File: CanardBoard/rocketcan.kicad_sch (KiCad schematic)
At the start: 21 parts, among them J6 G125-MH104M4-04AD000P, U15 TPS2521, U17 TCAN3413DDFR

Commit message: done
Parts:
- removed D19: RB520S30T1G, Diode_SMD:D_SOD-523, symbol Device:D_Schottky
- removed R28: 31.6k, Resistor_SMD:R_0402_1005Metric, symbol Device:R_Small_US
- removed R30: 100k, Resistor_SMD:R_0402_1005Metric, symbol Device_Custom:R_Small_US
- C51: symbol Device_Custom:C_Small -> Device:C_Small
- C52: renamed from C59; symbol Device_Custom:C_Small -> Device:C_Small
- C53: renamed from C52; symbol Device_Custom:C_Small -> Device:C_Small
- C54: renamed from C72; symbol Device_Custom:C_Small -> Device:C_Small
- C55: renamed from C73; symbol Device_Custom:C_Small -> Device:C_Small
- C56: renamed from C60; symbol Device_Custom:C_Small -> Device:C_Small
- R44: renamed from R56; symbol Device_Custom:R_Small_US -> Device:R_Small_US
- R45: renamed from R57; symbol Device_Custom:R_Small_US -> Device:R_Small_US
- R46: renamed from R58; symbol Device_Custom:R_Small_US -> Device:R_Small_US
- R47: renamed from R54; symbol Device_Custom:R_Small_US -> Device:R_Small_US
- R48: renamed from R43; footprint Resistor_SMD:R_0402_1005Metric -> Resistor_SMD:R_0805_2012Metric; symbol Device_Custom:R_Small_US -> Device:R_Small_US
- R49: renamed from R48; symbol Device_Custom:R_Small_US -> Device:R_Small_US
- renumbered D1 to D16, F2 to F8, F1 to F9, J6 to J10, U17 to U15, U15 to U16
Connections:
- net 5V_EXT_EN renamed EN_EXT_5V
- net 5V_EXT_FLT renamed FLT_EXT_5V

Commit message: changes
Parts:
- renumbered D16 to D18, R44 to R43, R45 to R44, R46 to R45, R47 to R46, R48 to R47, R49 to R48
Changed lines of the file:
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@@
 		(on_board yes)
 		(dnp yes)
-		(property "Reference" "R48"
+		(property "Reference" "R47"
 			(at 142.24 132.08 90)
 			(effects
@@
 			(project "CanardBoard"
 				(path "/605ab838-6b02-4cf5-a6b5-94a0cdb1b998/4fea5507-ad74-497c-bf16-b3654a0fa101"
-					(reference "R48")
+					(reference "R47")
 					(unit 1)
 				)
@@
 		(dnp no)
 		(fields_autoplaced yes)
-		(property "Reference" "#PWR0136"
+		(property "Reference" "#PWR0139"
 			(at 181.61 97.79 0)
 			(effects
@@
 			(project "CanardBoard"
 				(path "/605ab838-6b02-4cf5-a6b5-94a0cdb1b998/4fea5507-ad74-497c-bf16-b3654a0fa101"
-					(reference "#PWR0136")
+					(reference "#PWR0139")
 					(unit 1)
 				)
@@
 		(on_board yes)
 		(dnp no)
-		(property "Reference" "R47"
+		(property "Reference" "R46"
 			(at 133.35 86.36 90)
 			(effects
@@
 			(project "CanardBoard"
 				(path "/605ab838-6b02-4cf5-a6b5-94a0cdb1b998/4fea5507-ad74-497c-bf16-b3654a0fa101"
-					(reference "R47")
+					(reference "R46")
 					(unit 1)
 				)
@@
 		(dnp no)
 		(fields_autoplaced yes)
-		(property "Reference" "#PWR0124"
+		(property "Reference" "#PWR0127"
 			(at 74.93 87.63 0)
 			(effects
@@
 			(project "CanardBoard"
 				(path "/605ab838-6b02-4cf5-a6b5-94a0cdb1b998/4fea5507-ad74-497c-bf16-b3654a0fa101"
-					(reference "#PWR0124")
+					(reference "#PWR0127")
 					(unit 1)
 				)
@@
 		(dnp no)
 		(fields_autoplaced yes)
-		(property "Reference" "#PWR0137"
+		(property "Reference" "#PWR0140"
 			(at 189.23 97.79 0)
 			(effects
@@
 			(project "CanardBoard"
 				(path "/605ab838-6b02-4cf5-a6b5-94a0cdb1b998/4fea5507-ad74-497c-bf16-b3654a0fa101"
-					(reference "#PWR0137")
+					(reference "#PWR0140")
 					(unit 1)
 				)
@@
 		(dnp no)
 		(fields_autoplaced yes)
-		(property "Reference" "#PWR0126"
+		(property "Reference" "#PWR0129"
 			(at 81.28 149.86 0)
 			(effects
@@
 			(project "CanardBoard"
 				(path "/605ab838-6b02-4cf5-a6b5-94a0cdb1b998/4fea5507-ad74-497c-bf16-b3654a0fa101"
-					(reference "#PWR0126")
+					(reference "#PWR0129")
 					(unit 1)
 				)
@@
 		(dnp no)
 		(fields_autoplaced yes)
-		(property "Reference" "#PWR0131"
+		(property "Reference" "#PWR0134"
 			(at 125.73 129.54 0)
 			(effects
@@
 			(project "CanardBoard"
 				(path "/605ab838-6b02-4cf5-a6b5-94a0cdb1b998/4fea5507-ad74-497c-bf16-b3654a0fa101"
-					(reference "#PWR0131")
+					(reference "#PWR0134")
 					(unit 1)
 				)
@@
 		(dnp no)
 		(fields_autoplaced yes)
-		(property "Reference" "#PWR0134"
+		(property "Reference" "#PWR0137"
 			(at 156.21 161.29 0)
 			(effects
@@
 			(project "CanardBoard"
 				(path "/605ab838-6b02-4cf5-a6b5-94a0cdb1b998/4fea5507-ad74-497c-bf16-b3654a0fa101"
-					(reference "#PWR0134")
+					(reference "#PWR0137")
 					(unit 1)
 				)
@@
 		(on_board yes)
 		(dnp no)
-		(property "Reference" "R49"
+		(property "Reference" "R48"
 			(at 185.42 68.58 90)
 			(effects
@@
 			(project "CanardBoard"
 				(path "/605ab838-6b02-4cf5-a6b5-94a0cdb1b998/4fea5507-ad74-497c-bf16-b3654a0fa101"
-					(reference "R49")
+					(reference "R48")
 					(unit 1)
 				)
@@
 		(dnp no)
 		(fields_autoplaced yes)
-		(property "Reference" "#PWR0132"
+		(property "Reference" "#PWR0135"
 			(at 135.89 57.15 0)
 			(effects
@@
 			(project "CanardBoard"
 				(path "/605ab838-6b02-4cf5-a6b5-94a0cdb1b998/4fea5507-ad74-497c-bf16-b3654a0fa101"
-					(reference "#PWR0132")
+					(reference "#PWR0135")
 					(unit 1)
 				)
@@
 		(dnp no)
 		(fields_autoplaced yes)
-		(property "Reference" "#PWR0138"
+		(property "Reference" "#PWR0141"
 			(at 200.66 97.79 0)
 			(effects
@@
 			(project "CanardBoard"
 				(path "/605ab838-6b02-4cf5-a6b5-94a0cdb1b998/4fea5507-ad74-497c-bf16-b3654a0fa101"
-					(reference "#PWR0138")
+					(reference "#PWR0141")
 					(unit 1)
 				)
@@
 		(on_board yes)
 		(dnp no)
-		(property "Reference" "R44"
+		(property "Reference" "R43"
 			(at 113.03 71.12 90)
 			(effects
@@
 			(project "CanardBoard"
 				(path "/605ab838-6b02-4cf5-a6b5-94a0cdb1b998/4fea5507-ad74-497c-bf16-b3654a0fa101"
-					(reference "R44")
+					(reference "R43")
 					(unit 1)
 				)
@@
 		(dnp no)
 		(fields_autoplaced yes)
-		(property "Reference" "#PWR0127"
+		(property "Reference" "#PWR0130"
 			(at 90.17 54.61 0)
 			(effects
@@
 			(project "CanardBoard"
 				(path "/605ab838-6b02-4cf5-a6b5-94a0cdb1b998/4fea5507-ad74-497c-bf16-b3654a0fa101"
-					(reference "#PWR0127")
+					(reference "#PWR0130")
 					(unit 1)
 				)
@@
 		(dnp no)
 		(fields_autoplaced yes)
-		(property "Reference" "#PWR0123"
+		(property "Reference" "#PWR0126"
 			(at 74.93 54.61 0)
 			(effects
@@
 			(project "CanardBoard"
 				(path "/605ab838-6b02-4cf5-a6b5-94a0cdb1b998/4fea5507-ad74-497c-bf16-b3654a0fa101"
-					(reference "#PWR0123")
+					(reference "#PWR0126")
 					(unit 1)
 				)
@@
 		(dnp no)
 		(fields_autoplaced yes)
-		(property "Reference" "#PWR0125"
+		(property "Reference" "#PWR0128"
 			(at 81.28 114.3 0)
 			(effects
@@
 			(project "CanardBoard"
 				(path "/605ab838-6b02-4cf5-a6b5-94a0cdb1b998/4fea5507-ad74-497c-bf16-b3654a0fa101"
-					(reference "#PWR0125")
+					(reference "#PWR0128")
 					(unit 1)
 				)
@@
 		(dnp no)
 		(fields_autoplaced yes)
-		(property "Reference" "#PWR0130"
+		(property "Reference" "#PWR0133"
 			(at 116.84 114.3 0)
 			(effects
@@
 			(project "CanardBoard"
 				(path "/605ab838-6b02-4cf5-a6b5-94a0cdb1b998/4fea5507-ad74-497c-bf16-b3654a0fa101"
-					(reference "#PWR0130")
+					(reference "#PWR0133")
 					(unit 1)
 				)
@@
 		(on_board yes)
 		(dnp no)
-		(property "Reference" "R45"
+		(property "Reference" "R44"
 			(at 113.03 78.74 90)
 			(effects
@@
 			(project "CanardBoard"
 				(path "/605ab838-6b02-4cf5-a6b5-94a0cdb1b998/4fea5507-ad74-497c-bf16-b3654a0fa101"
-					(reference "R45")
+					(reference "R44")
 					(unit 1)
 				)
@@
 		(dnp no)
 		(fields_autoplaced yes)
-		(property "Reference" "#PWR0135"
+		(property "Reference" "#PWR0138"
 			(at 181.61 63.5 0)
 			(effects
@@
 			(project ""
 				(path "/605ab838-6b02-4cf5-a6b5-94a0cdb1b998/4fea5507-ad74-497c-bf16-b3654a0fa101"
-					(reference "#PWR0135")
+					(reference "#PWR0138")
 					(unit 1)
 				)
@@
 		(on_board yes)
 		(dnp no)
-		(property "Reference" "R46"
+		(property "Reference" "R45"
 			(at 133.35 59.69 90)
 			(effects
@@
 			(project "CanardBoard"
 				(path "/605ab838-6b02-4cf5-a6b5-94a0cdb1b998/4fea5507-ad74-497c-bf16-b3654a0fa101"
-					(reference "R46")
+					(reference "R45")
 					(unit 1)
 				)
@@
 		(dnp no)
 		(fields_autoplaced yes)
-		(property "Reference" "#PWR0139"
+		(property "Reference" "#PWR0142"
 			(at 205.74 78.74 0)
 			(effects
@@
 			(project "CanardBoard"
 				(path "/605ab838-6b02-4cf5-a6b5-94a0cdb1b998/4fea5507-ad74-497c-bf16-b3654a0fa101"
-					(reference "#PWR0139")
+					(reference "#PWR0142")
 					(unit 1)
 				)
@@
 		(dnp no)
 		(fields_autoplaced yes)
-		(property "Reference" "D16"
+		(property "Reference" "D18"
 			(at 162.56 144.7799 0)
 			(effects
@@
 			(project "CanardBoard"
 				(path "/605ab838-6b02-4cf5-a6b5-94a0cdb1b998/4fea5507-ad74-497c-bf16-b3654a0fa101"
-					(reference "D16")
+					(reference "D18")
 					(unit 1)
 				)
@@
 		(dnp no)
 		(fields_autoplaced yes)
-		(property "Reference" "#PWR0129"
+		(property "Reference" "#PWR0132"
 			(at 115.57 97.79 0)
 			(effects
@@
 			(project "CanardBoard"
 				(path "/605ab838-6b02-4cf5-a6b5-94a0cdb1b998/4fea5507-ad74-497c-bf16-b3654a0fa101"
-					(reference "#PWR0129")
+					(reference "#PWR0132")
 					(unit 1)
 				)
@@
 		(dnp no)
 		(fields_autoplaced yes)
-		(property "Reference" "#PWR0122"
+		(property "Reference" "#PWR0125"
 			(at 71.12 129.54 0)
 			(effects
@@
 			(project "CanardBoard"
 				(path "/605ab838-6b02-4cf5-a6b5-94a0cdb1b998/4fea5507-ad74-497c-bf16-b3654a0fa101"
-					(reference "#PWR0122")
+					(reference "#PWR0125")
 					(unit 1)
 				)
@@
 		(dnp no)
 		(fields_autoplaced yes)
-		(property "Reference" "#PWR0128"
+		(property "Reference" "#PWR0131"
 			(at 90.17 87.63 0)
 			(effects
@@
 			(project "CanardBoard"
 				(path "/605ab838-6b02-4cf5-a6b5-94a0cdb1b998/4fea5507-ad74-497c-bf16-b3654a0fa101"
-					(reference "#PWR0128")
+					(reference "#PWR0131")
 					(unit 1)
 				)
@@
 		(dnp no)
 		(fields_autoplaced yes)
-		(property "Reference" "#PWR0133"
+		(property "Reference" "#PWR0136"
 			(at 135.89 97.79 0)
 			(effects
@@
 			(project "CanardBoard"
 				(path "/605ab838-6b02-4cf5-a6b5-94a0cdb1b998/4fea5507-ad74-497c-bf16-b3654a0fa101"
-					(reference "#PWR0133")
-					(unit 1)
-				)
+					(reference "#PWR0136")
+					(unit 1)
+				)

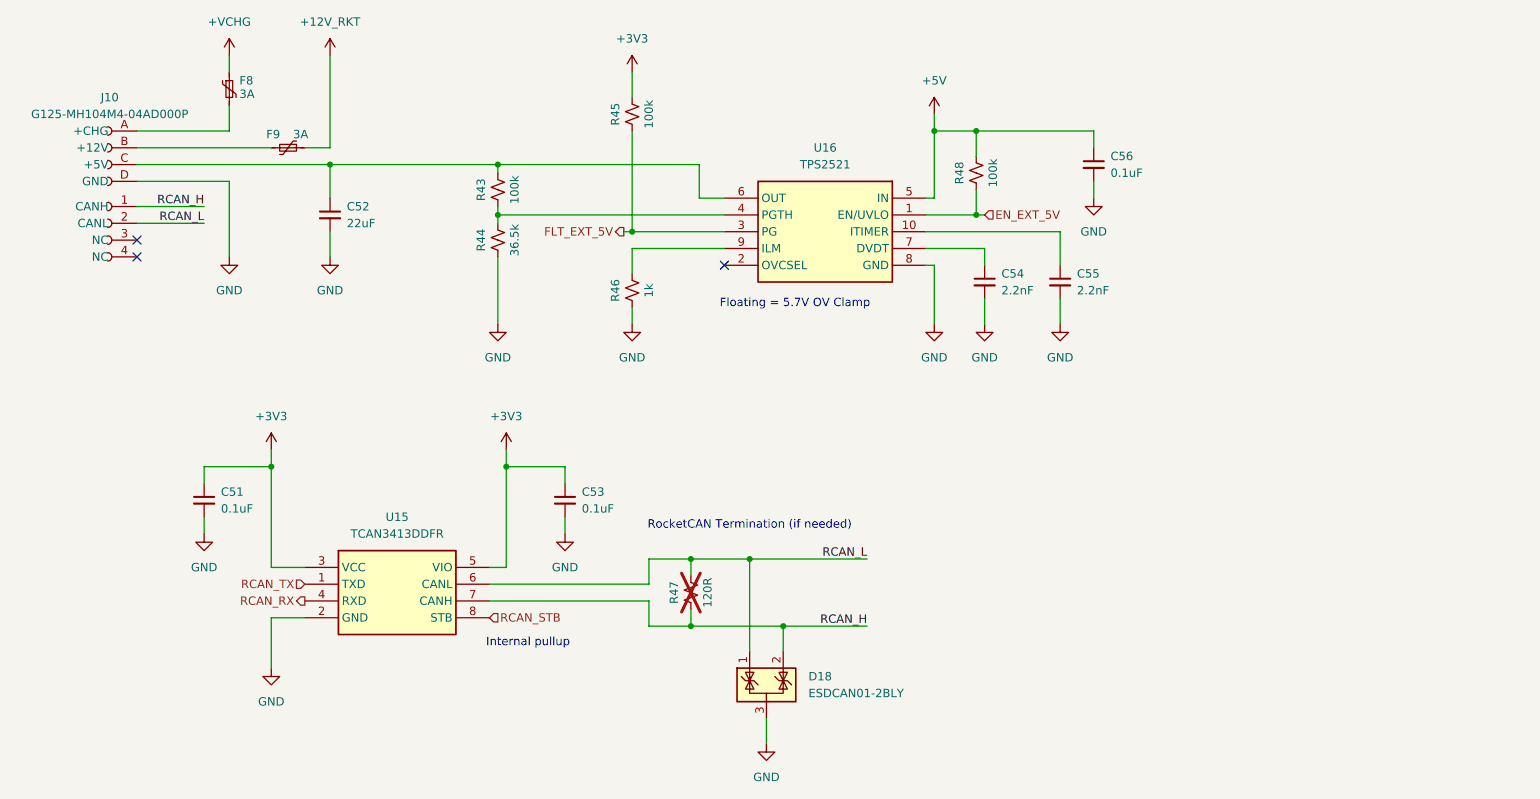
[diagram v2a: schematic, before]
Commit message: found new components to simplify and make board smaller
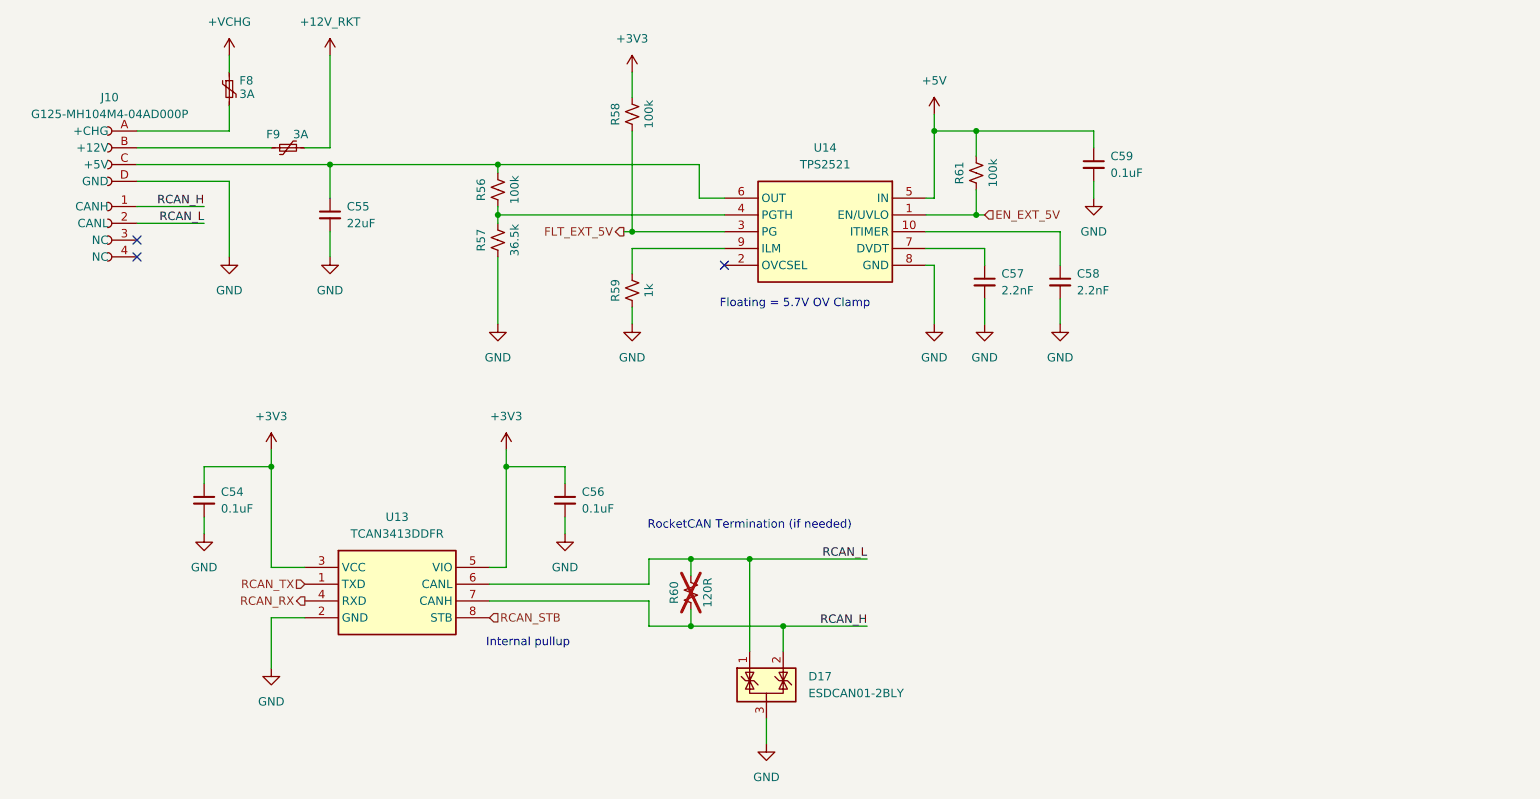
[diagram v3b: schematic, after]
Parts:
- renumbered C51 to C54, C52 to C55, C53 to C56, C54 to C57, C55 to C58, C56 to C59, D18 to D17, R43 to R56, R44 to R57, R45 to R58, R46 to R59, R47 to R60, R48 to R61, U15 to U13, U16 to U14

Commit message: work
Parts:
- renumbered C54 to C55, C55 to C56, C56 to C57, C57 to C58, C58 to C59, C59 to C60
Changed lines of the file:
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@@
 		(dnp no)
 		(fields_autoplaced yes)
-		(property "Reference" "C58"
+		(property "Reference" "C59"
 			(at 203.2 83.8262 0)
 			(effects
@@
 			(project "CanardBoard"
 				(path "/605ab838-6b02-4cf5-a6b5-94a0cdb1b998/4fea5507-ad74-497c-bf16-b3654a0fa101"
-					(reference "C58")
+					(reference "C59")
 					(unit 1)
 				)
@@
 		(dnp no)
 		(fields_autoplaced yes)
-		(property "Reference" "C56"
+		(property "Reference" "C57"
 			(at 128.27 116.8462 0)
 			(effects
@@
 			(project "CanardBoard"
 				(path "/605ab838-6b02-4cf5-a6b5-94a0cdb1b998/4fea5507-ad74-497c-bf16-b3654a0fa101"
-					(reference "C56")
+					(reference "C57")
 					(unit 1)
 				)
@@
 		(dnp no)
 		(fields_autoplaced yes)
-		(property "Reference" "C59"
+		(property "Reference" "C60"
 			(at 208.28 66.0462 0)
 			(effects
@@
 			(project "CanardBoard"
 				(path "/605ab838-6b02-4cf5-a6b5-94a0cdb1b998/4fea5507-ad74-497c-bf16-b3654a0fa101"
-					(reference "C59")
+					(reference "C60")
 					(unit 1)
 				)
@@
 		(dnp no)
 		(fields_autoplaced yes)
-		(property "Reference" "C57"
+		(property "Reference" "C58"
 			(at 191.77 83.8262 0)
 			(effects
@@
 			(project "CanardBoard"
 				(path "/605ab838-6b02-4cf5-a6b5-94a0cdb1b998/4fea5507-ad74-497c-bf16-b3654a0fa101"
-					(reference "C57")
+					(reference "C58")
 					(unit 1)
 				)
@@
 		(dnp no)
 		(fields_autoplaced yes)
-		(property "Reference" "C54"
+		(property "Reference" "C55"
 			(at 73.66 116.8462 0)
 			(effects
@@
 			(project "CanardBoard"
 				(path "/605ab838-6b02-4cf5-a6b5-94a0cdb1b998/4fea5507-ad74-497c-bf16-b3654a0fa101"
-					(reference "C54")
+					(reference "C55")
 					(unit 1)
 				)
@@
 		(dnp no)
 		(fields_autoplaced yes)
-		(property "Reference" "C55"
+		(property "Reference" "C56"
 			(at 92.71 73.6662 0)
 			(effects
@@
 			(project "CanardBoard"
 				(path "/605ab838-6b02-4cf5-a6b5-94a0cdb1b998/4fea5507-ad74-497c-bf16-b3654a0fa101"
-					(reference "C55")
-					(unit 1)
-				)
+					(reference "C56")
+					(unit 1)
+				)

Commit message: stuff
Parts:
- removed U14: TPS2521, canardboard:TPS2521, symbol canardboard:TPS2521
- added R62: 43.2k, Resistor_SMD:R_0402_1005Metric, symbol Device:R_Small_US
- added U14: TPS259472, canardboard:TPS25947xx, symbol canardboard:TPS259472
- C60: value 0.1uF -> 1uF
- R57: value 36.5k -> 34k
- R58: value 100k -> 681R
- R59: value 1k -> 100k
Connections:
- net FLT_EXT_5V is gone; now on net GND: R58.2
- net +3V3: now also R59.1; no longer R58.1
- net +5V: now also U14.5 (IN)
- net EN_EXT_5V: now also R62.1, U14.1 (EN/UVLO)
- net GND: now also R62.2, U14.8 (GND); no longer R59.2
- net at C59.1: now also U14.10 (ITIMER)
- net at C56.1, J10.C (+5V), R56.1: now also U14.6 (OUT)
- net at R56.2, R57.1: now also U14.4 (PGTH)
- net at C58.1: now also U14.7 (DVDT)
- new net: R58.1, U14.9 (ILM)
- new net PG_EXT_5V: R59.2, U14.3 (PG)

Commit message: more stuff
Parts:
- added C89: 22uF, Capacitor_SMD:C_0805_2012Metric, symbol Device:C_Small
- added C91: 0.1uF, Capacitor_SMD:C_0402_1005Metric, symbol Device:C_Small
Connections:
- net +5V: now also C91.1
- net GND: now also C89.2, C91.2
- net RKT_5V_OUT: now reaches C56.1, J10.C (+5V), R56.1, U14.6 (OUT)
- net RKT_5V_OUT: now also C89.1

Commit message: more work
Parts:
- added TP5: RCAN_H, TestPoint:TestPoint_Pad_D1.0mm, symbol Connector:TestPoint_Small
- added TP6: RCAN_L, TestPoint:TestPoint_Pad_D1.0mm, symbol Connector:TestPoint_Small
- added TP7: RCAN_RX, TestPoint:TestPoint_Pad_D1.0mm, symbol Connector:TestPoint_Small
- added TP8: RCAN_TX, TestPoint:TestPoint_Pad_D1.0mm, symbol Connector:TestPoint_Small
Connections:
- net RCAN_H: now also TP5.1
- net RCAN_L: now also TP6.1
- net RCAN_RX: now also TP7.1
- net RCAN_TX: now also TP8.1

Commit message: fix some things and assign LCSC PNs
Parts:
- C55, C57, C91: LCSC Part # C49678 -> C85858
- C56, C89: LCSC Part # C49678 -> C86816
- C58, C59: value 2.2nF -> 10nF; LCSC Part # C49678 -> C91601
- C60: LCSC Part # C49678 -> C77007
- D17: LCSC Part # (none) -> C1976606
- R56, R57, R58, R59, R60, R61, R62: LCSC Part # C17630 -> (none)
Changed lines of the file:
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@@
 			)
 		)
-		(property "LCSC Part #" "C17630"
+		(property "LCSC Part #" ""
 			(at 144.78 132.08 0)
 			(effects
@@
 			)
 		)
-		(property "LCSC Part #" "C49678"
+		(property "LCSC Part #" "C85858"
 			(at 125.73 118.11 0)
 			(effects
@@
 			)
 		)
-		(property "LCSC Part #" "C17630"
+		(property "LCSC Part #" ""
 			(at 127 81.28 0)
 			(effects
@@
 			)
 		)
-		(property "LCSC Part #" "C17630"
+		(property "LCSC Part #" ""
 			(at 195.58 76.2 0)
 			(effects
@@
 			)
 		)
-		(property "LCSC Part #" "C49678"
+		(property "LCSC Part #" "C77007"
 			(at 212.09 72.39 0)
 			(effects
@@
 			)
 		)
-		(property "LCSC Part #" "C17630"
+		(property "LCSC Part #" ""
 			(at 114.3 71.12 0)
 			(effects
@@
 			)
 		)
-		(property "LCSC Part #" "C49678"
+		(property "LCSC Part #" "C86816"
 			(at 101.6 74.93 0)
 			(effects
@@
 			)
 		)
-		(property "LCSC Part #" "C17630"
+		(property "LCSC Part #" ""
 			(at 132.08 62.23 0)
 			(effects
@@
 			)
 		)
-		(property "LCSC Part #" "C17630"
+		(property "LCSC Part #" ""
 			(at 195.58 66.04 0)
 			(effects
@@
 			)
 		)
-		(property "LCSC Part #" "C49678"
+		(property "LCSC Part #" "C85858"
 			(at 71.12 118.11 0)
 			(effects
@@
 			)
 		)
-		(property "Datasheet" "https://www.onsemi.com/pub_link/Collateral/NUP2105L-D.PDF"
+		(property "Datasheet" ""
 			(at 159.385 142.875 0)
 			(effects
@@
 			)
 		)
+		(property "LCSC Part #" "C1976606"
+			(at 156.21 146.05 0)
+			(effects
+				(font
+					(size 1.27 1.27)
+				)
+				(hide yes)
+			)
+		)
 		(pin "2"
 		)
@@
 			)
 		)
-		(property "LCSC Part #" "C17630"
+		(property "LCSC Part #" ""
 			(at 114.3 80.01 0)
 			(effects
@@
 			)
 		)
-		(property "LCSC Part #" "C49678"
+		(property "LCSC Part #" "C86816"
 			(at 90.17 74.93 0)
 			(effects
@@
 			)
 		)
-		(property "Value" "2.2nF"
+		(property "Value" "10nF"
 			(at 184.15 80.0162 0)
 			(effects
@@
 			)
 		)
-		(property "LCSC Part #" "C49678"
+		(property "LCSC Part #" "C91601"
 			(at 181.61 78.74 0)
 			(effects
@@
 			)
 		)
-		(property "Value" "2.2nF"
+		(property "Value" "10nF"
 			(at 173.99 80.0162 0)
 			(effects
@@
 			)
 		)
-		(property "LCSC Part #" "C49678"
+		(property "LCSC Part #" "C91601"
 			(at 171.45 78.74 0)
 			(effects
@@
 			)
 		)
-		(property "LCSC Part #" "C49678"
+		(property "LCSC Part #" "C85858"
 			(at 220.98 72.39 0)
 			(effects
